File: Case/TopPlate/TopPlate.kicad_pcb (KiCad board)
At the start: 2 copper layers, 156.9 x 100.9 mm, 4 parts

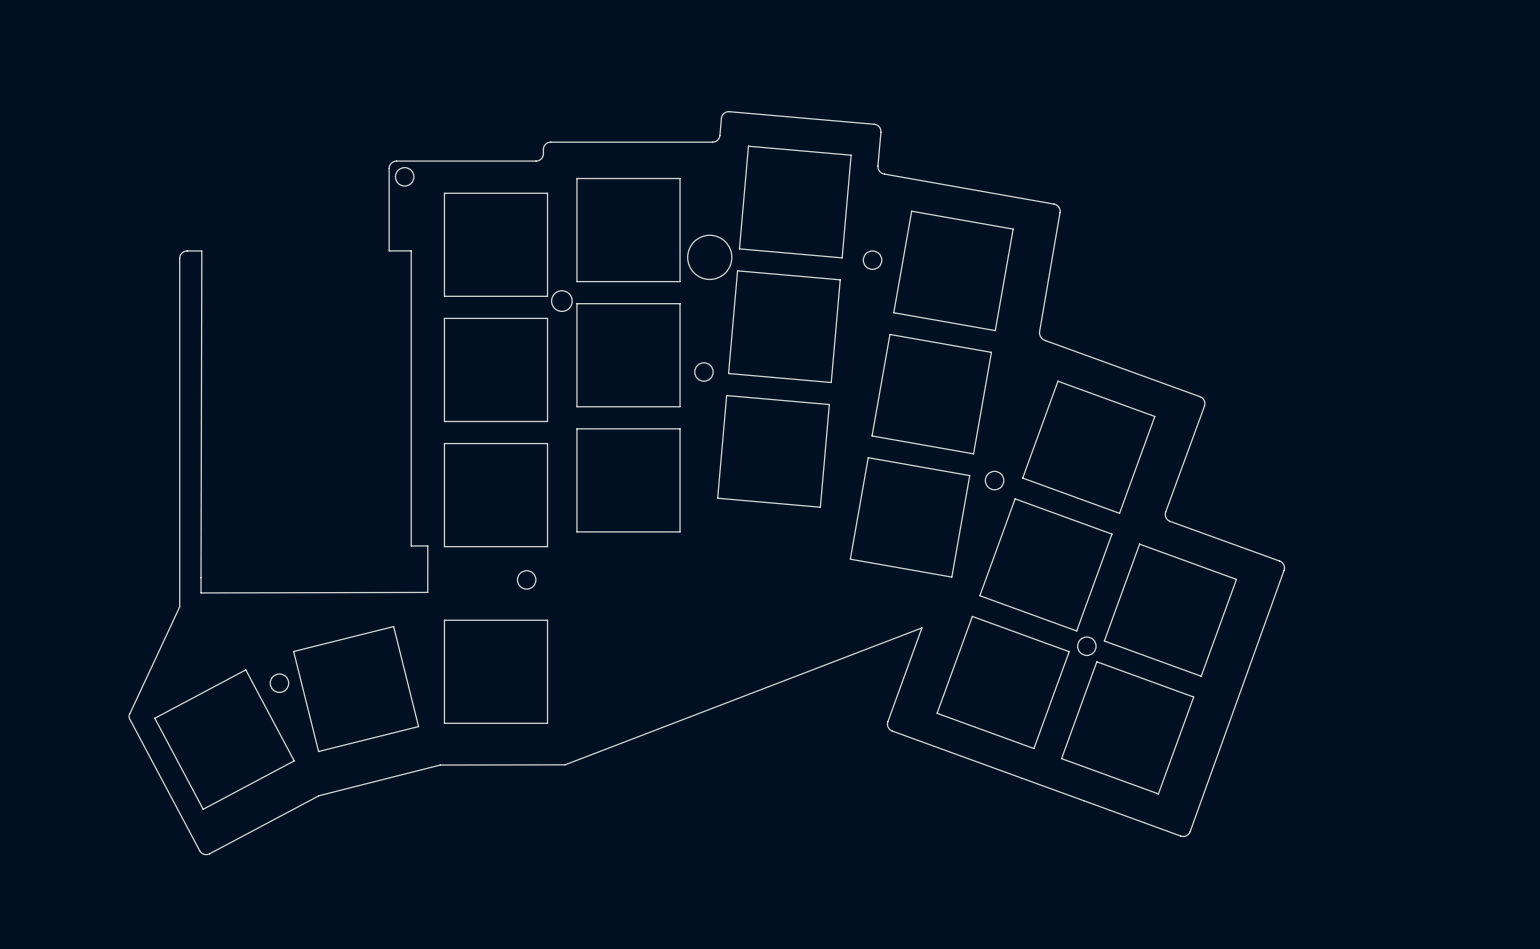
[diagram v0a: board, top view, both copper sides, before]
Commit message: add logo and better through holes
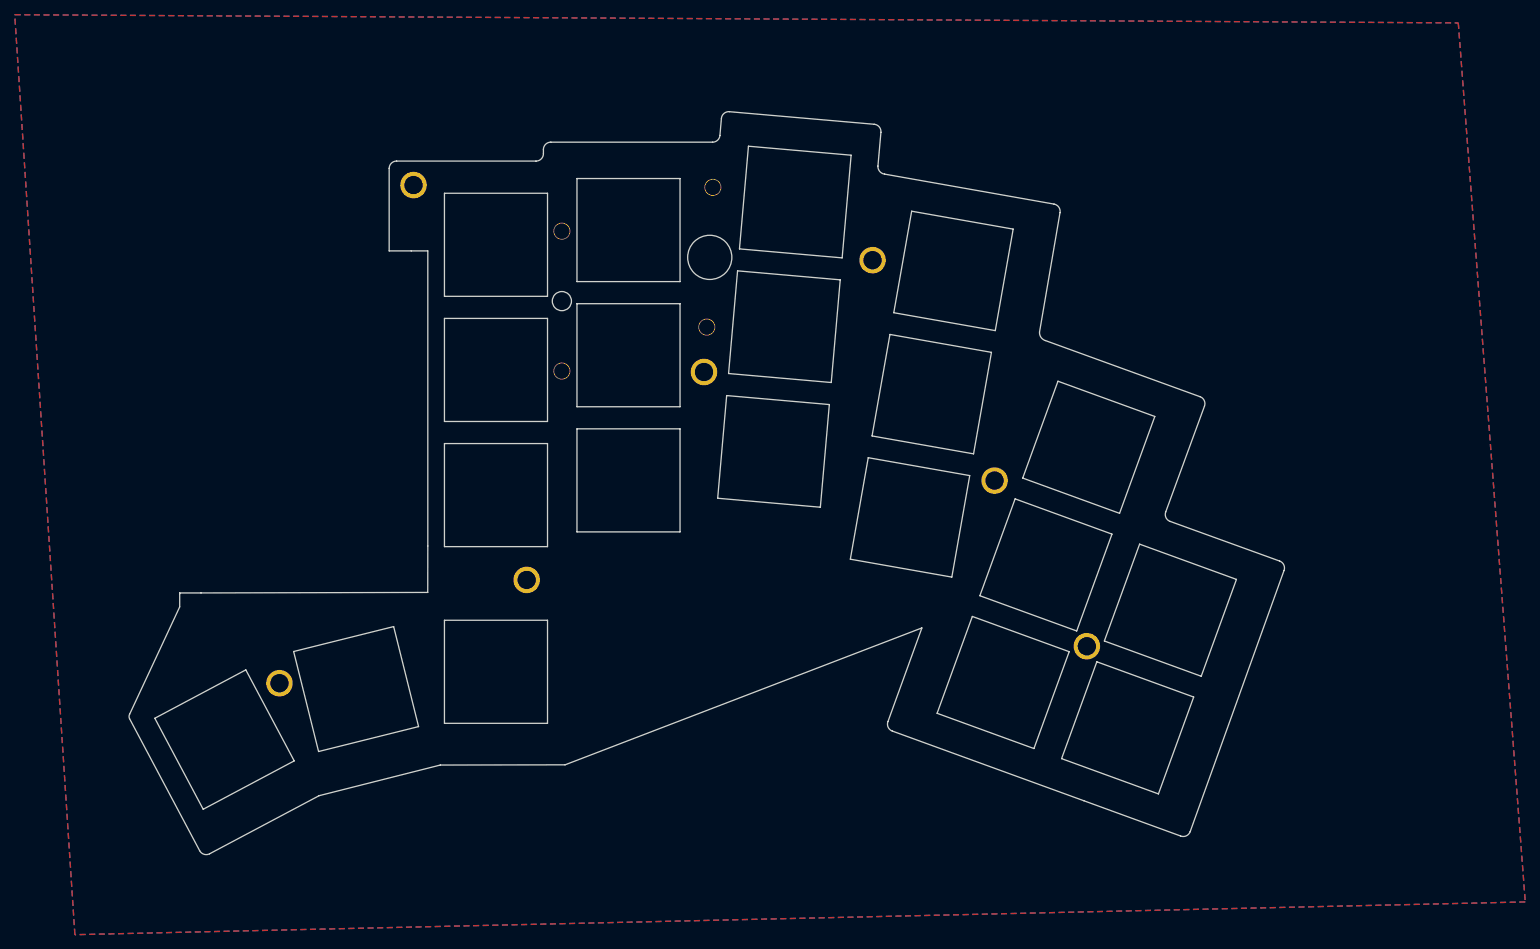
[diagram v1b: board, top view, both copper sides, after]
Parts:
- added ?: , kbd:M2_Hole_TH, F.Cu at (155.6, 80.5)
- added ?: , kbd:M2_Hole_TH, F.Cu at (98.0, 122.8)
- added ?: , kbd:M2_Hole_TH, F.Cu at (195.1, 95.3)
- added ?: , kbd:M2_Hole_TH, F.Cu at (178.5, 65.3)
- added ?: , kbd:M2_Hole_TH, F.Cu at (207.6, 117.8)
- added ?: , kbd:M2_Hole_TH, F.Cu at (116.2, 55.1)
- added ?: , kbd:M2_Hole_TH, F.Cu at (131.6, 108.8)
- added U10: Hole, Buzzard:HOLE_M2_TH, F.Cu at (156.0, 74.4)
- added U11: Hole, Buzzard:HOLE_M2_TH, F.Cu at (136.3, 80.4)
- added U12: Hole, Buzzard:HOLE_M2_TH, F.Cu at (136.3, 61.4)
- added U13: Hole, Buzzard:HOLE_M2_TH, F.Cu at (156.8, 55.5)
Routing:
- added copper zone on B.Cu, net (none)
- added copper zone on F.Cu, net (none)
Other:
- outline, holes or cut-outs redrawn

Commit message: Some fine tuning and silkmask improvments
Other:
- outline, holes or cut-outs redrawn
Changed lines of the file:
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@@
   (gr_circle (center 156.416703 64.958833) (end 159.416703 64.958833) (layer "Edge.Cuts") (width 0.1) (fill none))
   (gr_arc (start 156.8 48.31) (end 156.8 49.310799) (angle -85.14690361) (layer "Edge.Cuts") (width 0.1))
-  (gr_line (start 87.315523 110.54) (end 84.42 110.54) (layer "Edge.Cuts") (width 0.1))
   (gr_line (start 185.231968 115.292483) (end 180.621064 128.015035) (layer "Edge.Cuts") (width 0.1))
   (gr_circle (center 136.33 70.9) (end 137.63 70.9) (layer "Edge.Cuts") (width 0.1) (fill none))
@@
   (gr_arc (start 181.558926 128.362589) (end 181.211372 129.300451) (angle 90) (layer "Edge.Cuts") (width 0.1))
   (gr_line (start 159.089873 45.172207) (end 178.764908 46.881038) (layer "Edge.Cuts") (width 0.1))
-  (gr_line (start 84.42 110.66) (end 84.42 110.54) (layer "Edge.Cuts") (width 0.1))
-  (gr_line (start 84.42 112.43) (end 84.42 110.66) (layer "Edge.Cuts") (width 0.1))
   (gr_line (start 115.87 64.080539) (end 112.871242 64.080539) (layer "Edge.Cuts") (width 0.1))
+  (gr_line (start 84.42 112.43) (end 87.31 110.54) (layer "Edge.Cuts") (width 0.1))
   (gr_arc (start 203.00253 58.712247) (end 203.188762 57.723566) (angle 89.33252867) (layer "Edge.Cuts") (width 0.1))
   (gr_poly (pts
